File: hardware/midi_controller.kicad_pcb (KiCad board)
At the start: 2 copper layers, 16 parts, among them J1 DIN5, J2 DIN5, J3 CONN_03, J4 CONN_04, J5 CONN_03, J6 CONN_05, J7 CONN_03, J8 CONN_03, J9 CONN_03, U1 6N137

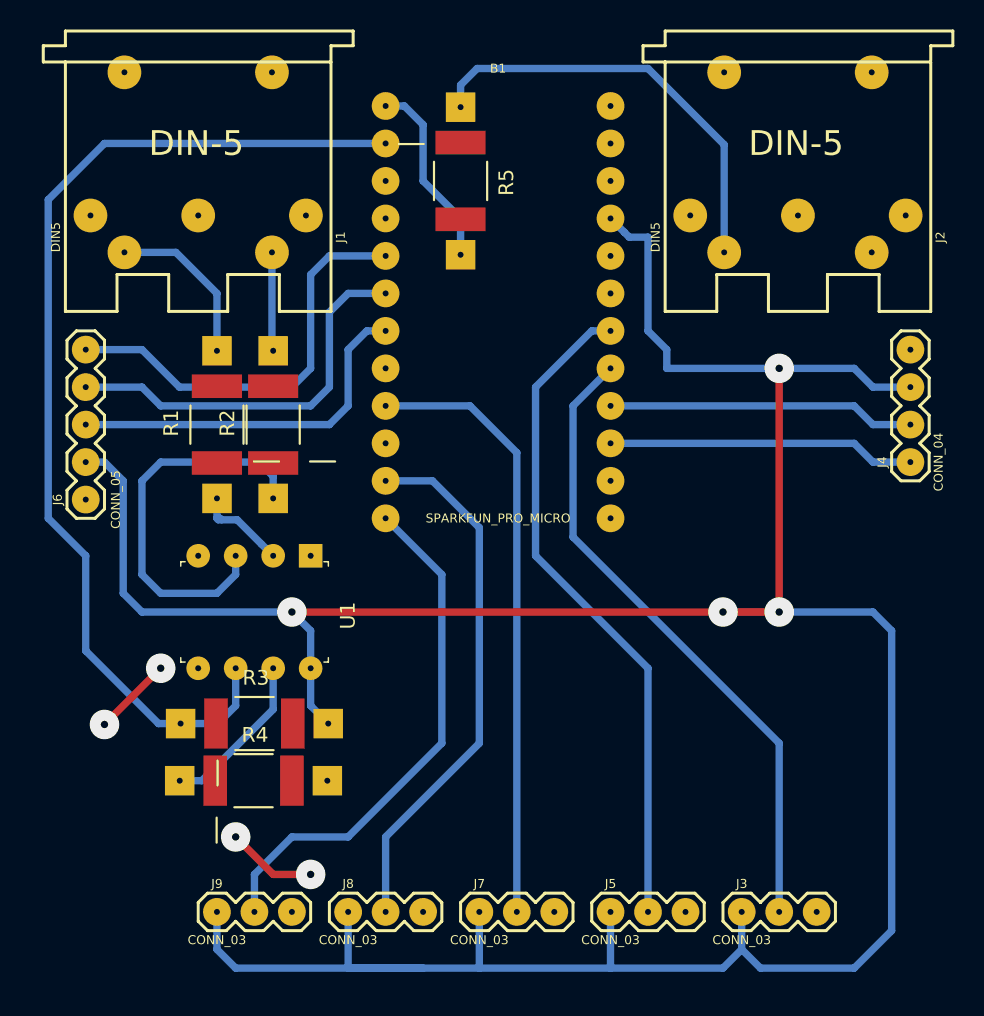
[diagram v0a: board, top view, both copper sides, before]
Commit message: fix analog pins and remove redundant resistor
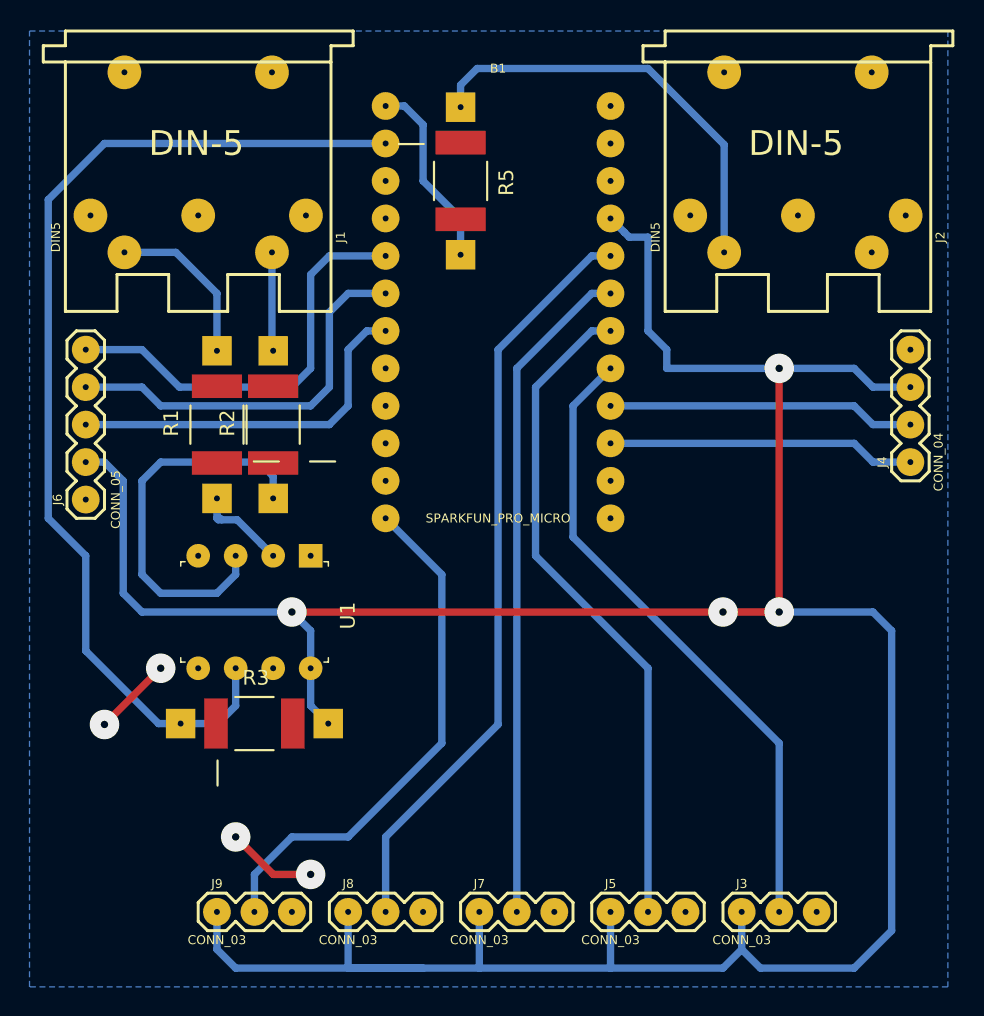
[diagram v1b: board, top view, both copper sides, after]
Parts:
- removed R4: RESISTOR0402, Resistors_Universal:Resistor_SMD+THTuniversal_2512_RM10_HandSoldering_RevA_Date25Jun2010
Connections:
- J7 pad 2: Net-(B1-Pad9) -> Net-(B1-Pad19)
- J8 pad 2: Net-(B1-Pad11) -> Net-(B1-Pad20)
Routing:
- net Net-(B1-Pad20): track 0.00 -> 51.5 mm
- net Net-(B1-Pad19): track 0.00 -> 45.3 mm
- net Net-(B1-Pad9): track 41.3 -> 0.00 mm
- net Net-(B1-Pad11): track 36.3 -> 0.00 mm
- net Net-(U1-Pad7): track 11.1 -> 0.00 mm
- added copper zone on B.Cu, net GND
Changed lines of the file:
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@@
     (thickness 1.6)
     (drawings 0)
-    (tracks 145)
+    (tracks 142)
     (zones 0)
-    (modules 16)
+    (modules 15)
     (nets 39)
   )
   (page A4)
   (layers
-    (0 F.Cu signal hide)
+    (0 F.Cu signal)
     (31 B.Cu signal)
     (32 B.Adhes user hide)
@@
   (net 34 "Net-(R1-Pad1)")
   (net 35 "Net-(R2-Pad1)")
-  (net 36 "Net-(R4-Pad1)")
-  (net 37 "Net-(U1-Pad4)")
-  (net 38 "Net-(U1-Pad1)")
+  (net 36 "Net-(U1-Pad4)")
+  (net 37 "Net-(U1-Pad1)")
+  (net 38 "Net-(U1-Pad7)")
   (net_class Default "This is the default net class."
     (clearance 0.2)
@@
     (add_net "Net-(R1-Pad1)")
     (add_net "Net-(R2-Pad1)")
-    (add_net "Net-(R4-Pad1)")
     (add_net "Net-(U1-Pad1)")
     (add_net "Net-(U1-Pad4)")
+    (add_net "Net-(U1-Pad7)")
   )
   (module Sparkfun_Connectors:1X03 (layer F.Cu)
@@
       (net 2 GND) (solder_mask_margin 0.1016))
     (pad 2 thru_hole circle (at 2.54 0) (size 1.8796 1.8796) (drill 0.4) (layers *.Cu *.Mask)
-      (net 14 "Net-(B1-Pad11)") (solder_mask_margin 0.1016))
+      (net 5 "Net-(B1-Pad20)") (solder_mask_margin 0.1016))
     (pad 1 thru_hole circle (at 0 0) (size 1.8796 1.8796) (drill 0.4) (layers *.Cu *.Mask)
       (net 4 "Net-(B1-Pad21)") (solder_mask_margin 0.1016))
@@
       (net 2 GND) (solder_mask_margin 0.1016))
     (pad 2 thru_hole circle (at 2.54 0) (size 1.8796 1.8796) (drill 0.4) (layers *.Cu *.Mask)
-      (net 16 "Net-(B1-Pad9)") (solder_mask_margin 0.1016))
+      (net 6 "Net-(B1-Pad19)") (solder_mask_margin 0.1016))
     (pad 1 thru_hole circle (at 0 0) (size 1.8796 1.8796) (drill 0.4) (layers *.Cu *.Mask)
       (net 4 "Net-(B1-Pad21)") (solder_mask_margin 0.1016))
@@
       (net 4 "Net-(B1-Pad21)"))
     (pad 7 thru_hole circle (at 7.62 2.54 270) (size 1.6 1.6) (drill 0.4) (layers *.Cu *.Mask)
-      (net 36 "Net-(R4-Pad1)"))
+      (net 38 "Net-(U1-Pad7)"))
     (pad 6 thru_hole circle (at 7.62 5.08 270) (size 1.6 1.6) (drill 0.4) (layers *.Cu *.Mask)
       (net 23 "Net-(B1-Pad2)"))
@@
       (net 2 GND))
     (pad 4 thru_hole circle (at 0 7.62 270) (size 1.6 1.6) (drill 0.4) (layers *.Cu *.Mask)
-      (net 37 "Net-(U1-Pad4)"))
+      (net 36 "Net-(U1-Pad4)"))
     (pad 3 thru_hole circle (at 0 5.08 270) (size 1.6 1.6) (drill 0.4) (layers *.Cu *.Mask)
       (net 35 "Net-(R2-Pad1)"))
@@
       (net 34 "Net-(R1-Pad1)"))
     (pad 1 thru_hole rect (at 0 0 270) (size 1.6 1.6) (drill 0.4) (layers *.Cu *.Mask)
-      (net 38 "Net-(U1-Pad1)"))
+      (net 37 "Net-(U1-Pad1)"))
     (model ${KISYS3DMOD}/Housings_DIP.3dshapes/DIP-8_W7.62mm.wrl
       (at (xyz 0 0 0))
@@
     (pad 2 thru_hole rect (at 5.00126 0 180) (size 1.99898 1.99898) (drill 0.4) (layers *.Cu *.Mask)
       (net 4 "Net-(B1-Pad21)"))
-  )
-  (module Resistors_Universal:Resistor_SMD+THTuniversal_2512_RM10_HandSoldering_RevA_Date25Jun2010 (layer F.Cu)
-    (at 126.93904 86.36)
-    (descr "Resistor, SMD+THT, 2512, RM10, Hand soldering,")
-    (tags "Resistor, SMD+THT, 2512, RM10, Hand soldering,")
-    (fp_text reference R4 (at 0.09906 -3.0988) (layer F.SilkS)
-      (effects (font (size 1 1) (thickness 0.15)))
-    )
-    (fp_text value RESISTOR0402 (at -0.39878 4.20116) (layer F.Fab)
-      (effects (font (size 1 1) (thickness 0.15)))
-    )
-    (fp_circle (center 0 0) (end 0.20066 0) (layer F.Adhes) (width 0.381))
-    (fp_circle (center 0 0) (end 0.50038 0) (layer F.Adhes) (width 0.381))
-    (fp_circle (center 0 0) (end 0.8001 0) (layer F.Adhes) (width 0.381))
-    (fp_line (start -2.49936 2.49936) (end -2.49936 4.20116) (layer F.SilkS) (width 0.15))
-    (fp_line (start 1.30048 -1.80086) (end -1.30048 -1.80086) (layer F.SilkS) (width 0.15))
-    (fp_line (start -1.30048 1.80086) (end 1.30048 1.80086) (layer F.SilkS) (width 0.15))
-    (pad 2 thru_hole rect (at 5.00126 0 180) (size 1.99898 1.99898) (drill 0.4) (layers *.Cu *.Mask)
-      (net 2 GND))
-    (pad 1 thru_hole rect (at -5.00126 0 180) (size 1.99898 1.99898) (drill 0.4) (layers *.Cu *.Mask)
-      (net 36 "Net-(R4-Pad1)"))
-    (pad 2 smd rect (at 2.60096 0) (size 1.6002 3.40106) (layers F.Cu F.Paste F.Mask)
-      (net 2 GND))
-    (pad 1 smd rect (at -2.60096 0) (size 1.6002 3.40106) (layers F.Cu F.Paste F.Mask)
-      (net 36 "Net-(R4-Pad1)"))
   )
   (module Resistors_Universal:Resistor_SMD+THTuniversal_2512_RM10_HandSoldering_RevA_Date25Jun2010 (layer F.Cu)
@@
   (via (at 162.56 58.42) (size 2) (drill 0.5) (layers F.Cu B.Cu) (net 4))
   (segment (start 162.56 58.42) (end 162.56 74.93) (width 0.5) (layer F.Cu) (net 4))
+  (segment (start 149.86 53.34) (end 151.13 53.34) (width 0.5) (layer B.Cu) (net 6))
+  (segment (start 144.78 58.42) (end 149.86 53.34) (width 0.5) (layer B.Cu) (net 6))
+  (segment (start 144.78 95.25) (end 144.78 58.42) (width 0.5) (layer B.Cu) (net 6))
   (segment (start 149.86 55.88) (end 151.13 55.88) (width 0.5) (layer B.Cu) (net 7))
   (segment (start 146.05 71.12) (end 146.05 59.69) (width 0.5) (layer B.Cu) (net 7))
@@
   (segment (start 139.7 72.39) (end 135.89 68.58) (width 0.5) (layer B.Cu) (net 13))
   (segment (start 139.7 83.82) (end 139.7 72.39) (width 0.5) (layer B.Cu) (net 13))
-  (segment (start 135.89 90.17) (end 142.24 83.82) (width 0.5) (layer B.Cu) (net 14))
-  (segment (start 135.89 95.25) (end 135.89 90.17) (width 0.5) (layer B.Cu) (net 14))
-  (segment (start 135.89 66.04) (end 139.065 66.04) (width 0.5) (layer B.Cu) (net 14))
-  (segment (start 139.065 66.04) (end 142.24 69.215) (width 0.5) (layer B.Cu) (net 14))
-  (segment (start 142.24 69.215) (end 142.24 83.82) (width 0.5) (layer B.Cu) (net 14))
-  (segment (start 141.605 60.96) (end 135.89 60.96) (width 0.5) (layer B.Cu) (net 16))
-  (segment (start 144.78 64.135) (end 141.605 60.96) (width 0.5) (layer B.Cu) (net 16))
-  (segment (start 144.78 95.25) (end 144.78 64.135) (width 0.5) (layer B.Cu) (net 16))
+  (segment (start 135.89 95.25) (end 135.89 90.17) (width 0.5) (layer B.Cu) (net 5))
+  (segment (start 135.89 90.17) (end 143.51 82.55) (width 0.5) (layer B.Cu) (net 5))
+  (segment (start 143.51 82.55) (end 143.51 57.15) (width 0.5) (layer B.Cu) (net 5))
+  (segment (start 143.51 57.15) (end 149.86 50.8) (width 0.5) (layer B.Cu) (net 5))
+  (segment (start 149.86 50.8) (end 151.13 50.8) (width 0.5) (layer B.Cu) (net 5))
   (segment (start 134.62 55.88) (end 135.89 55.88) (width 0.5) (layer B.Cu) (net 18))
   (segment (start 133.35 57.15) (end 134.62 55.88) (width 0.5) (layer B.Cu) (net 18))
@@
   (segment (start 124.46 73.66) (end 125.73 72.39) (width 0.5) (layer B.Cu) (net 35))
   (segment (start 125.73 72.39) (end 125.73 71.12) (width 0.5) (layer B.Cu) (net 35))
-  (segment (start 123.43727 86.36) (end 128.27 81.52727) (width 0.5) (layer B.Cu) (net 36))
-  (segment (start 121.93778 86.36) (end 123.43727 86.36) (width 0.5) (layer B.Cu) (net 36))
-  (segment (start 128.27 81.52727) (end 128.27 78.74) (width 0.5) (layer B.Cu) (net 36))
+  (zone (net 2) (net_name GND) (layer B.Cu) (hatch edge 0.508)
+    (connect_pads yes (clearance 0.508))
+    (min_thickness 0.254)
+    (fill yes (arc_segments 32) (thermal_gap 0.508) (thermal_bridge_width 0.508))
+    (polygon
+      (pts
+        (xy 111.76 35.56) (xy 173.99 35.56) (xy 173.99 100.33) (xy 111.76 100.33)
+      )
+    )
+  )
 )
